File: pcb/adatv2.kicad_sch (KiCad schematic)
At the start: 0 parts

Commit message: Further schematic capture
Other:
- sheet IO renamed IO main
- added sheet FPGA and clock generators (fpga.kicad_sch)
- added sheet IO board (io_board.kicad_sch)
- note added: "Subschematics:"
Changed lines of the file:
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@@
 		(comment 1 "Drawn by Łukasz Świszcz")
 	)
-	(sheet
-		(at 134.62 100.33)
-		(size 12.7 12.7)
-		(exclude_from_sim no)
-		(in_bom yes)
-		(on_board yes)
-		(dnp no)
-		(fields_autoplaced yes)
-		(stroke
-			(width 0.1524)
-			(type solid)
-		)
-		(fill
-			(color 255 227 161 1.0000)
-		)
-		(property "Sheetname" "IO"
-			(at 134.62 99.6184 0)
+	(text "Subschematics:"
+		(exclude_from_sim no)
+		(at 177.292 28.702 0)
+		(effects
+			(font
+				(size 2.54 2.54)
+				(thickness 0.254)
+				(bold yes)
+			)
+			(justify left)
+		)
+	)
+	(sheet
+		(at 177.8 35.56)
+		(size 12.7 12.7)
+		(exclude_from_sim no)
+		(in_bom yes)
+		(on_board yes)
+		(dnp no)
+		(fields_autoplaced yes)
+		(stroke
+			(width 0.1524)
+			(type solid)
+		)
+		(fill
+			(color 255 227 161 1.0000)
+		)
+		(property "Sheetname" "IO board"
+			(at 177.8 34.8484 0)
+			(effects
+				(font
+					(size 1.27 1.27)
+				)
+				(justify left bottom)
+			)
+		)
+		(property "Sheetfile" "io_board.kicad_sch"
+			(at 177.8 48.8446 0)
+			(effects
+				(font
+					(size 1.27 1.27)
+				)
+				(justify left top)
+			)
+		)
+		(instances
+			(project "adatv2"
+				(path "/81929cdc-f9fd-4c47-8b7e-bc8597104756"
+					(page "2")
+				)
+			)
+		)
+	)
+	(sheet
+		(at 177.8 111.76)
+		(size 12.7 12.7)
+		(exclude_from_sim no)
+		(in_bom yes)
+		(on_board yes)
+		(dnp no)
+		(fields_autoplaced yes)
+		(stroke
+			(width 0.1524)
+			(type solid)
+		)
+		(fill
+			(color 255 227 161 1.0000)
+		)
+		(property "Sheetname" "IO main"
+			(at 177.8 111.0484 0)
 			(effects
 				(font
@@
 		)
 		(property "Sheetfile" "io.kicad_sch"
-			(at 134.62 113.6146 0)
+			(at 177.8 125.0446 0)
+			(effects
+				(font
+					(size 1.27 1.27)
+				)
+				(justify left top)
+			)
+		)
+		(instances
+			(project "adatv2"
+				(path "/81929cdc-f9fd-4c47-8b7e-bc8597104756"
+					(page "6")
+				)
+			)
+		)
+	)
+	(sheet
+		(at 177.8 54.61)
+		(size 12.7 12.7)
+		(exclude_from_sim no)
+		(in_bom yes)
+		(on_board yes)
+		(dnp no)
+		(fields_autoplaced yes)
+		(stroke
+			(width 0.1524)
+			(type solid)
+		)
+		(fill
+			(color 255 227 161 1.0000)
+		)
+		(property "Sheetname" "Power Supply"
+			(at 177.8 53.8984 0)
+			(effects
+				(font
+					(size 1.27 1.27)
+				)
+				(justify left bottom)
+			)
+		)
+		(property "Sheetfile" "power_supply.kicad_sch"
+			(at 177.8 67.8946 0)
+			(effects
+				(font
+					(size 1.27 1.27)
+				)
+				(justify left top)
+			)
+		)
+		(instances
+			(project "adatv2"
+				(path "/81929cdc-f9fd-4c47-8b7e-bc8597104756"
+					(page "3")
+				)
+			)
+		)
+	)
+	(sheet
+		(at 177.8 132.08)
+		(size 12.7 12.7)
+		(exclude_from_sim no)
+		(in_bom yes)
+		(on_board yes)
+		(dnp no)
+		(fields_autoplaced yes)
+		(stroke
+			(width 0.1524)
+			(type solid)
+		)
+		(fill
+			(color 255 227 161 1.0000)
+		)
+		(property "Sheetname" "Display board"
+			(at 177.8 131.3684 0)
+			(effects
+				(font
+					(size 1.27 1.27)
+				)
+				(justify left bottom)
+			)
+		)
+		(property "Sheetfile" "display_board.kicad_sch"
+			(at 177.8 145.3646 0)
+			(effects
+				(font
+					(size 1.27 1.27)
+				)
+				(justify left top)
+			)
+		)
+		(instances
+			(project "adatv2"
+				(path "/81929cdc-f9fd-4c47-8b7e-bc8597104756"
+					(page "7")
+				)
+			)
+		)
+	)
+	(sheet
+		(at 177.8 73.66)
+		(size 12.7 12.7)
+		(exclude_from_sim no)
+		(in_bom yes)
+		(on_board yes)
+		(dnp no)
+		(fields_autoplaced yes)
+		(stroke
+			(width 0.1524)
+			(type solid)
+		)
+		(fill
+			(color 255 227 161 1.0000)
+		)
+		(property "Sheetname" "MCU, USB and FPGA config"
+			(at 177.8 72.9484 0)
+			(effects
+				(font
+					(size 1.27 1.27)
+				)
+				(justify left bottom)
+			)
+		)
+		(property "Sheetfile" "main_board.kicad_sch"
+			(at 177.8 86.9446 0)
 			(effects
 				(font
@@
 	)
 	(sheet
-		(at 134.62 62.23)
-		(size 12.7 12.7)
-		(exclude_from_sim no)
-		(in_bom yes)
-		(on_board yes)
-		(dnp no)
-		(fields_autoplaced yes)
-		(stroke
-			(width 0.1524)
-			(type solid)
-		)
-		(fill
-			(color 255 227 161 1.0000)
-		)
-		(property "Sheetname" "Power Supply"
-			(at 134.62 61.5184 0)
-			(effects
-				(font
-					(size 1.27 1.27)
-				)
-				(justify left bottom)
-			)
-		)
-		(property "Sheetfile" "power_supply.kicad_sch"
-			(at 134.62 75.5146 0)
-			(effects
-				(font
-					(size 1.27 1.27)
-				)
-				(justify left top)
-			)
-		)
-		(instances
-			(project "adatv2"
-				(path "/81929cdc-f9fd-4c47-8b7e-bc8597104756"
-					(page "2")
-				)
-			)
-		)
-	)
-	(sheet
-		(at 134.62 120.65)
-		(size 12.7 12.7)
-		(exclude_from_sim no)
-		(in_bom yes)
-		(on_board yes)
-		(dnp no)
-		(fields_autoplaced yes)
-		(stroke
-			(width 0.1524)
-			(type solid)
-		)
-		(fill
-			(color 255 227 161 1.0000)
-		)
-		(property "Sheetname" "Display board"
-			(at 134.62 119.9384 0)
-			(effects
-				(font
-					(size 1.27 1.27)
-				)
-				(justify left bottom)
-			)
-		)
-		(property "Sheetfile" "display_board.kicad_sch"
-			(at 134.62 133.9346 0)
+		(at 177.8 92.71)
+		(size 12.7 12.7)
+		(exclude_from_sim no)
+		(in_bom yes)
+		(on_board yes)
+		(dnp no)
+		(fields_autoplaced yes)
+		(stroke
+			(width 0.1524)
+			(type solid)
+		)
+		(fill
+			(color 255 227 161 1.0000)
+		)
+		(property "Sheetname" "FPGA and clock generators"
+			(at 177.8 91.9984 0)
+			(effects
+				(font
+					(size 1.27 1.27)
+				)
+				(justify left bottom)
+			)
+		)
+		(property "Sheetfile" "fpga.kicad_sch"
+			(at 177.8 105.9946 0)
 			(effects
 				(font
@@
 				)
 			)
-		)
-	)
-	(sheet
-		(at 134.62 81.28)
-		(size 12.7 12.7)
-		(exclude_from_sim no)
-		(in_bom yes)
-		(on_board yes)
-		(dnp no)
-		(fields_autoplaced yes)
-		(stroke
-			(width 0.1524)
-			(type solid)
-		)
-		(fill
-			(color 255 227 161 1.0000)
-		)
-		(property "Sheetname" "MCU, USB and FPGA config"
-			(at 134.62 80.5684 0)
-			(effects
-				(font
-					(size 1.27 1.27)
-				)
-				(justify left bottom)
-			)
-		)
-		(property "Sheetfile" "main_board.kicad_sch"
-			(at 134.62 94.5646 0)
-			(effects
-				(font
-					(size 1.27 1.27)
-				)
-				(justify left top)
-			)
-		)
-		(instances
-			(project "adatv2"
-				(path "/81929cdc-f9fd-4c47-8b7e-bc8597104756"
-					(page "3")
-				)
-			)

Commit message: Further schematic capture
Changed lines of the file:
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@@
 	(text "Subschematics:"
 		(exclude_from_sim no)
-		(at 177.292 28.702 0)
+		(at 177.292 28.448 0)
 		(effects
 			(font
@@
 		)
 	)
+	(polyline
+		(pts
+			(xy 177.8 30.48) (xy 278.13 30.48)
+		)
+		(stroke
+			(width 0.254)
+			(type solid)
+		)
+	)
 	(sheet
 		(at 177.8 35.56)
@@
 				(font
 					(size 1.27 1.27)
+					(thickness 0.254)
+					(bold yes)
 				)
 				(justify left bottom)
@@
 				(font
 					(size 1.27 1.27)
+					(thickness 0.254)
+					(bold yes)
 				)
 				(justify left bottom)
@@
 				(font
 					(size 1.27 1.27)
+					(thickness 0.254)
+					(bold yes)
 				)
 				(justify left bottom)
@@
 				(font
 					(size 1.27 1.27)
+					(thickness 0.254)
+					(bold yes)
 				)
 				(justify left bottom)
@@
 				(font
 					(size 1.27 1.27)
+					(thickness 0.254)
+					(bold yes)
 				)
 				(justify left bottom)
@@
 				(font
 					(size 1.27 1.27)
-				)
-				(justify left bottom)
+					(thickness 0.254)
+					(bold yes)
+				)
+				(justify left bottom)

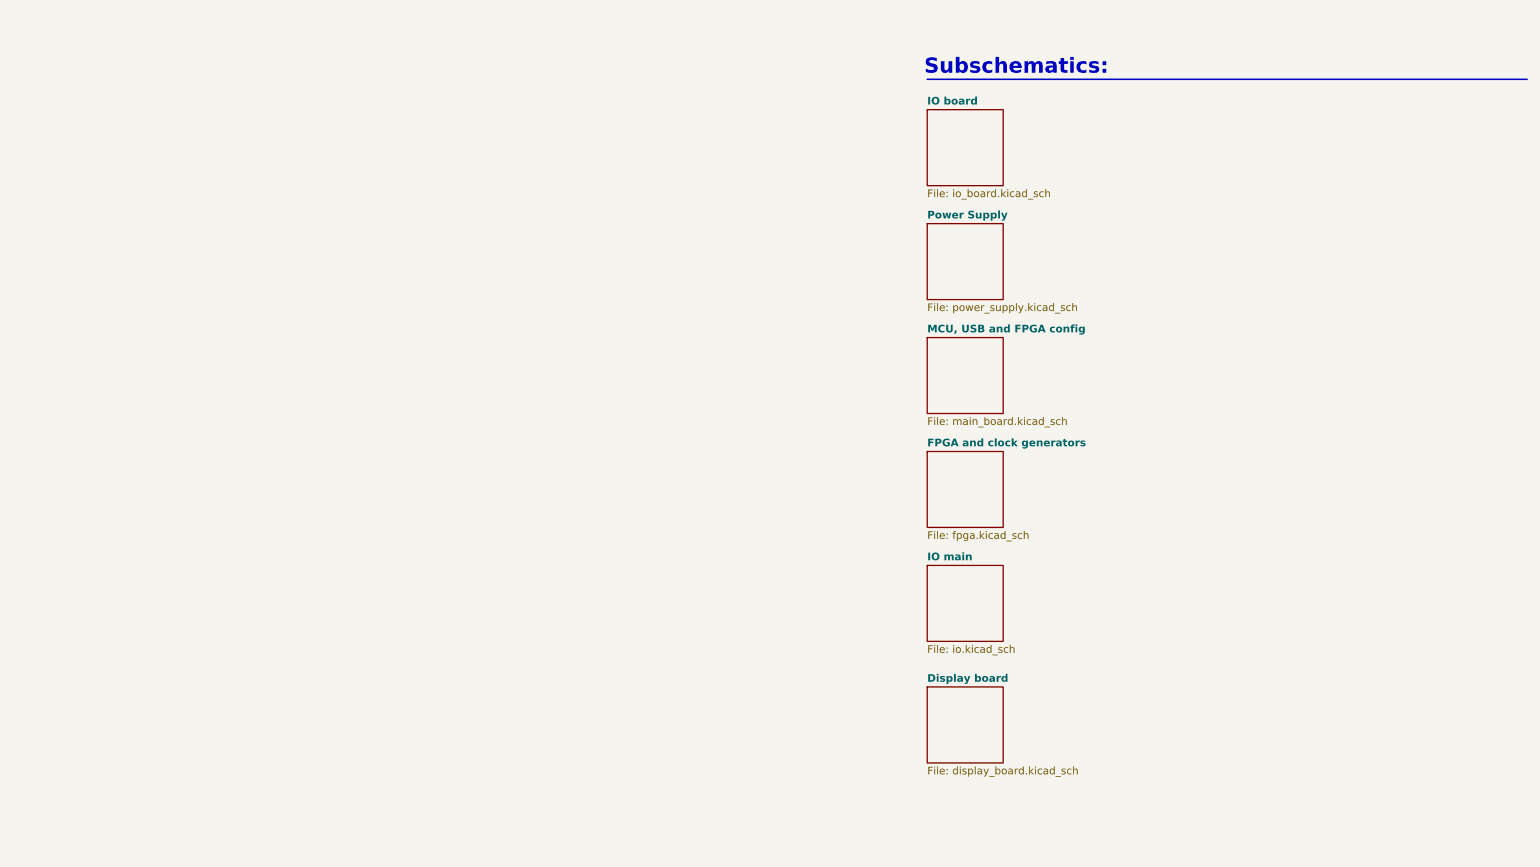
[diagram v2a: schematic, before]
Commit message: Assign most of the footprints to schematic components
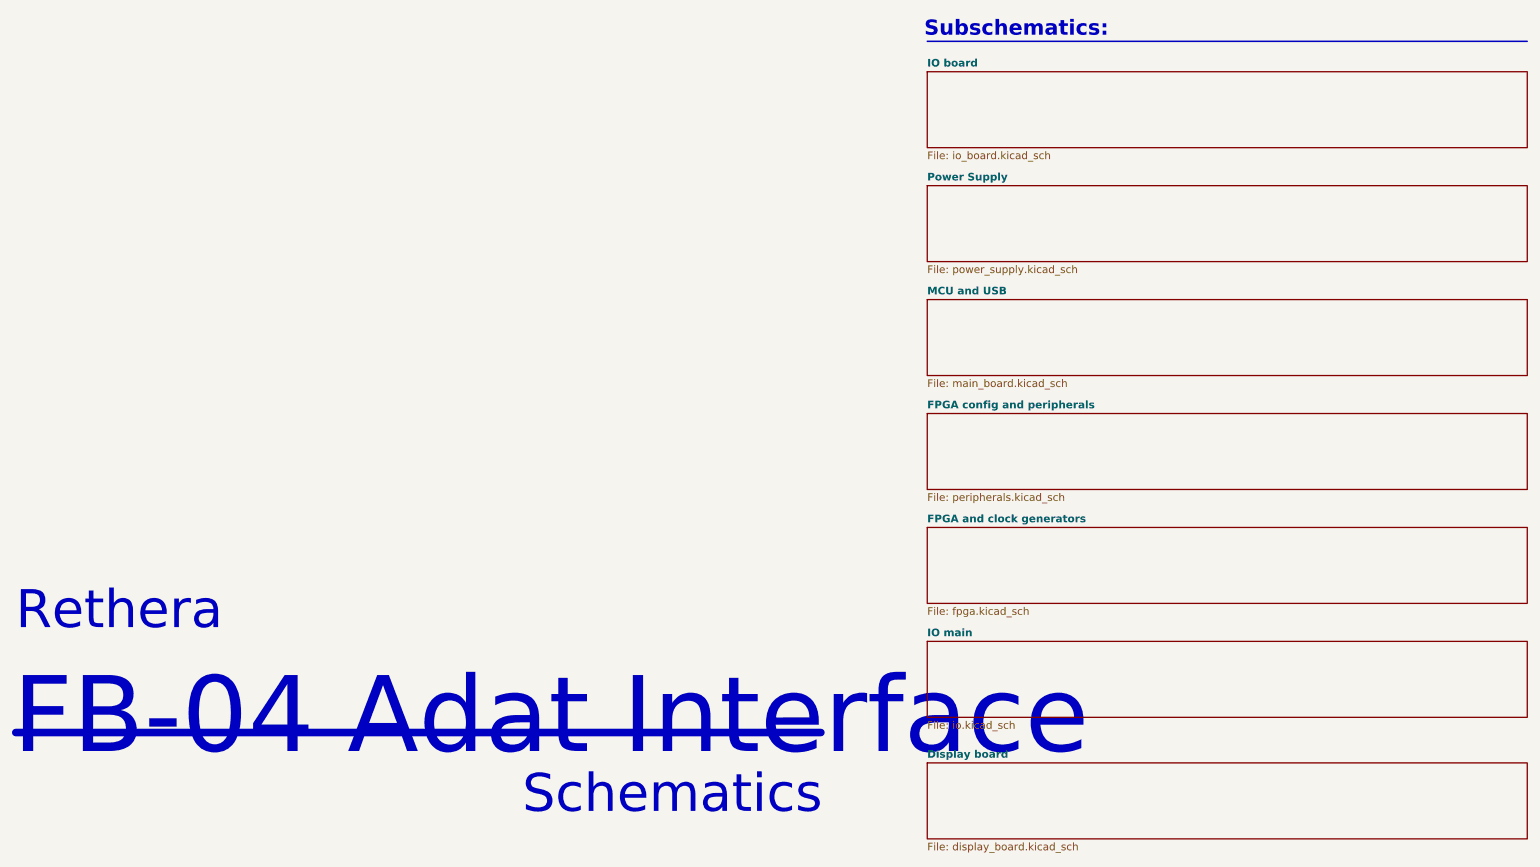
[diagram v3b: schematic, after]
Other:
- sheet MCU, USB and FPGA config renamed MCU and USB
- added sheet FPGA config and peripherals (peripherals.kicad_sch)
- note added: "FB-04 Adat Interface"
- note added: "Rethera"
- note added: "Schematics"
